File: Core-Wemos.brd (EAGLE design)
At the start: 86.5 x 100 mm, 50 parts, among them J2 CONNECTOR-GROVE-4P-2.0-347013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, J3 IO4

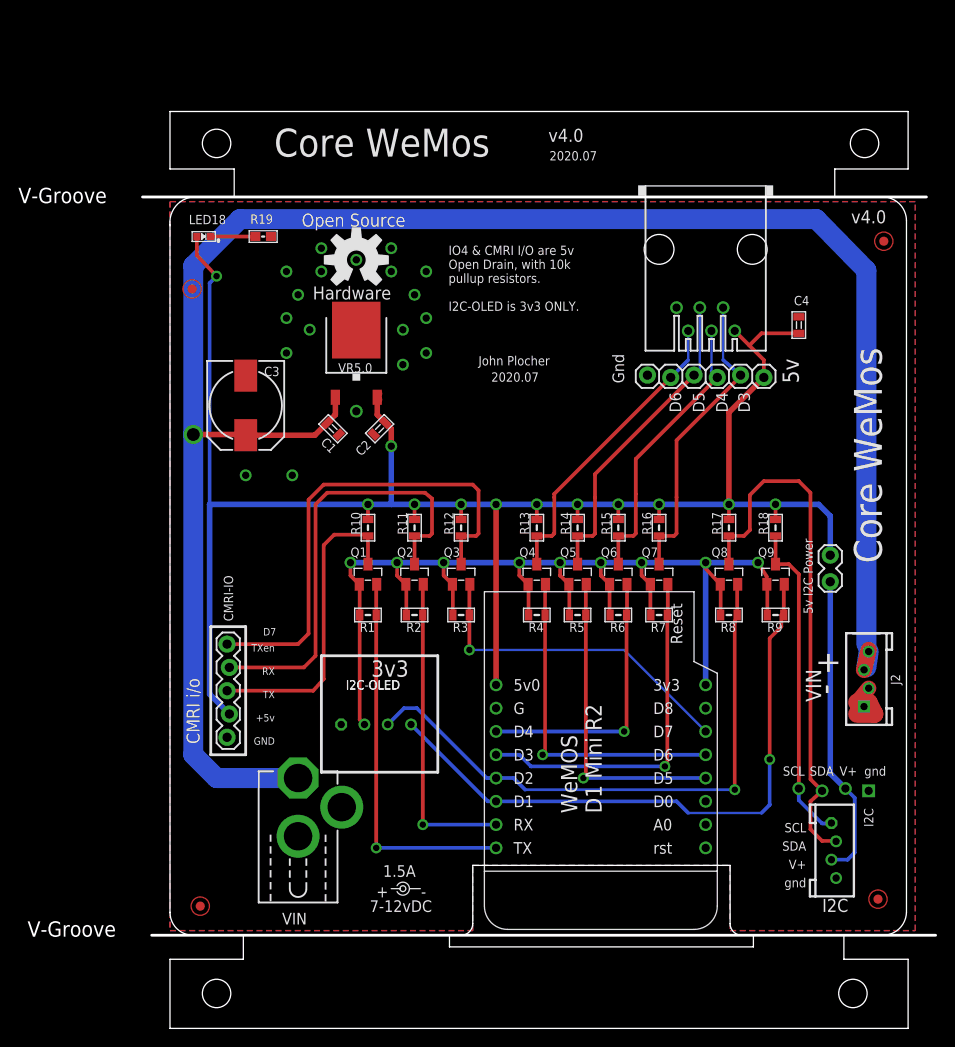
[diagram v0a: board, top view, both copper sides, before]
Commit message: Moved OLED, added 1x4 0.100 VIN
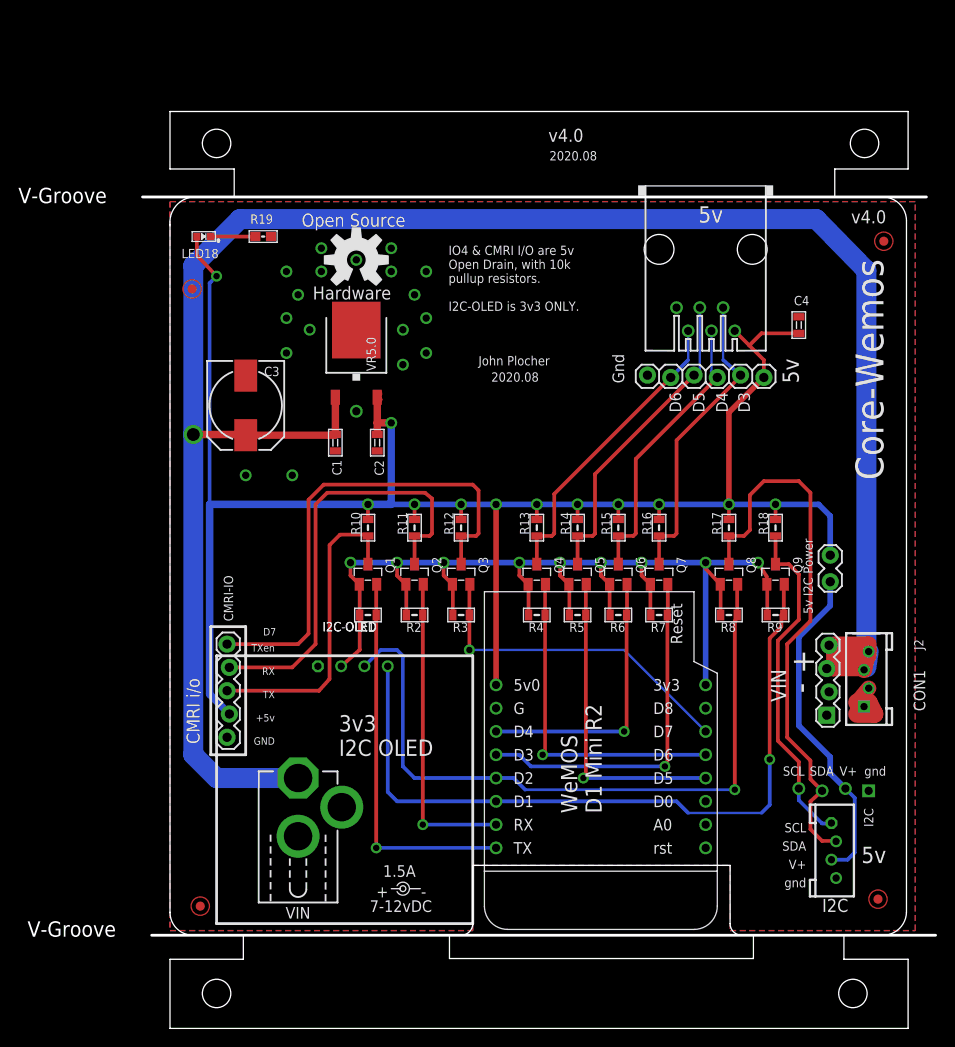
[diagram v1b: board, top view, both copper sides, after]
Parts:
- added CON1: (no value), SPCoast:1X04_LOCK
- moved I2C-OLED 6.84 mm to (19.9, 29.3)
- moved C1 1.55 mm to (18.0, 53.7), turned to 270 degrees
- moved C2 1.55 mm to (22.6, 53.7), turned to 270 degrees
- turned LED18 to 180 degrees
- turned Q1 to 270 degrees
- turned Q2 to 270 degrees
- turned Q3 to 270 degrees
- turned Q4 to 270 degrees
- turned Q5 to 270 degrees
- turned Q6 to 270 degrees
- turned Q7 to 270 degrees
- turned Q8 to 270 degrees
- turned Q9 to 270 degrees
- turned VR5.0 to 90 degrees
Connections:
- net +9V: now also CON1.3, CON1.4
- net GND: now also CON1.1, CON1.2
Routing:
- net +9V: track 208.0 -> 226.6 mm
- net SCL: track 68.3 -> 81.5 mm
- net SDA: track 65.2 -> 77.5 mm
- net +3V3: track 125.2 -> 119.6 mm
- net N$44: track 33.5 -> 36.3 mm
- net VCCIO: track 202.0 -> 204.1 mm
- net SDAH: track 58.3 -> 60.4 mm
- net SCLH: track 35.5 -> 37.4 mm
- net RXH: track 48.8 -> 48.1 mm
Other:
- board text added: "2020.08"
- board text added: "3v3 I2C OLED"
- board text added: ">DRAWING_NAME"
- board text removed: "2020.07"
- board text removed: "3v3"
- board text removed: "Core WeMos"

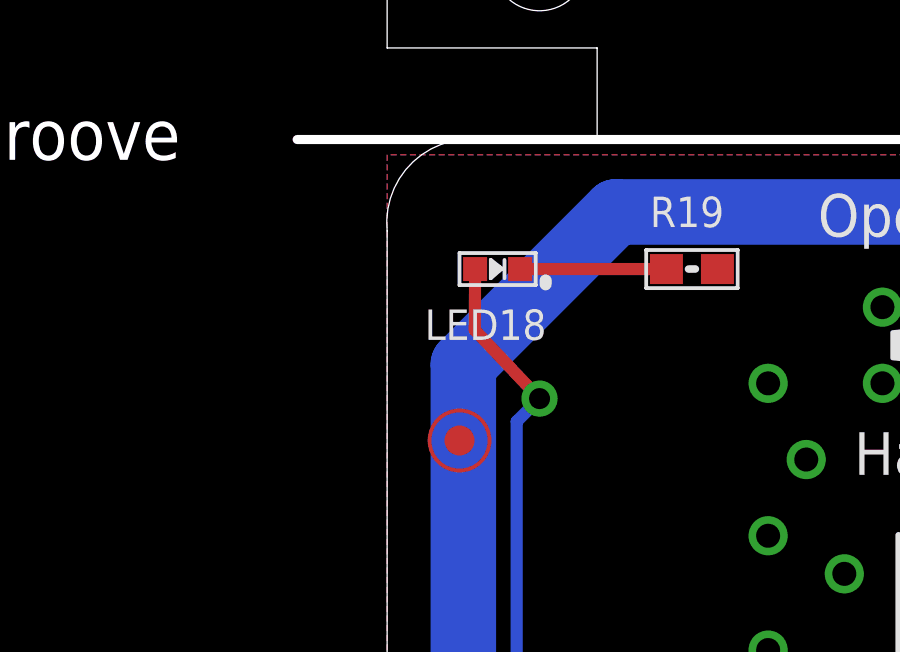
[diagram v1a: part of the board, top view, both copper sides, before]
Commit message: Renamed/Moved FIDs
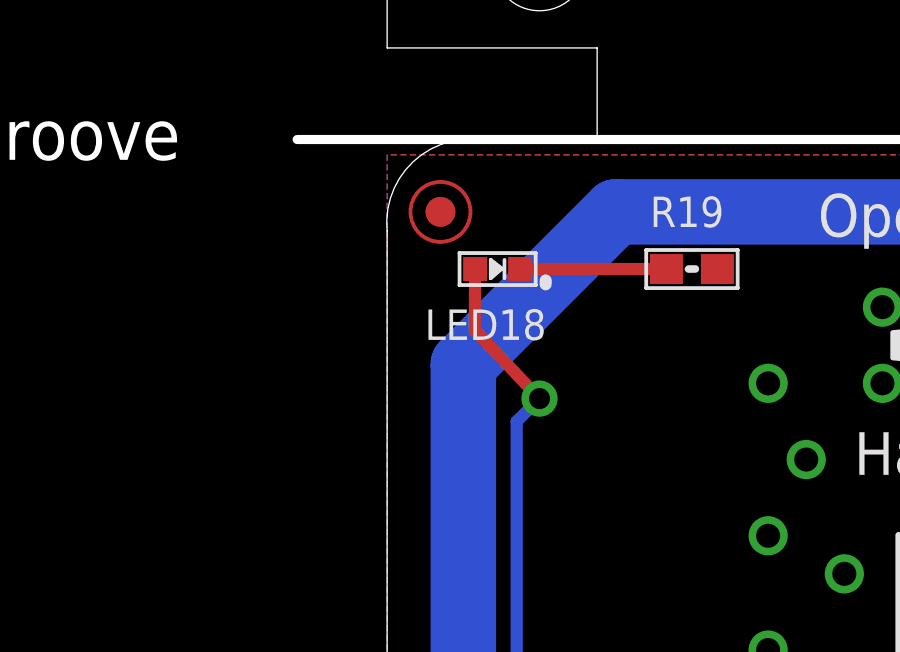
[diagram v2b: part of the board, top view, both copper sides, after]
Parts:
- removed FID3: FIDUCIAL, SPCoast:FIDUCIAL_1MM
- added FID-UL: FIDUCIAL, SPCoast:FIDUCIAL_1MM
- renumbered FID1 to FID-LR, FID2 to FID-LL, FID4 to FID-UR
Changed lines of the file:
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@@
 <setting verticaltext="up"/>
 </settings>
-<grid distance="50" unitdist="mil" unit="mil" style="dots" multiple="2" display="yes" altdistance="5" altunitdist="mil" altunit="mil"/>
+<grid distance="50" unitdist="mil" unit="mil" style="dots" multiple="2" display="yes" altdistance="25" altunitdist="mil" altunit="mil"/>
 <layers>
 <layer number="1" name="Top" color="4" fill="1" visible="yes" active="yes"/>
@@
 <attribute name="NAME" x="6.8834" y="34.2392" size="1.016" layer="25" ratio="10" rot="R90"/>
 </element>
-<element name="FID3" library="SPCoast" package="FIDUCIAL_1MM" value="FIDUCIAL" x="2.413" y="70.485" smashed="yes"/>
-<element name="FID1" library="SPCoast" package="FIDUCIAL_1MM" value="FIDUCIAL" x="77.216" y="3.937" smashed="yes"/>
-<element name="FID2" library="SPCoast" package="FIDUCIAL_1MM" value="FIDUCIAL" x="3.302" y="3.175" smashed="yes"/>
-<element name="FID4" library="SPCoast" package="FIDUCIAL_1MM" value="FIDUCIAL" x="77.851" y="75.692" smashed="yes"/>
+<element name="FID-UL" library="SPCoast" package="FIDUCIAL_1MM" value="FIDUCIAL" x="1.778" y="78.105" smashed="yes"/>
+<element name="FID-LR" library="SPCoast" package="FIDUCIAL_1MM" value="FIDUCIAL" x="77.216" y="3.937" smashed="yes"/>
+<element name="FID-LL" library="SPCoast" package="FIDUCIAL_1MM" value="FIDUCIAL" x="3.302" y="3.175" smashed="yes"/>
+<element name="FID-UR" library="SPCoast" package="FIDUCIAL_1MM" value="FIDUCIAL" x="77.851" y="75.692" smashed="yes"/>
 <element name="I2C-OLED" library="SPCoast" package="I2C-NOOUTLINE" value="" x="19.939" y="29.337" smashed="yes" rot="R180">
 <attribute name="NAME" x="16.637" y="33.147" size="1.016" layer="25" font="vector" ratio="11"/>

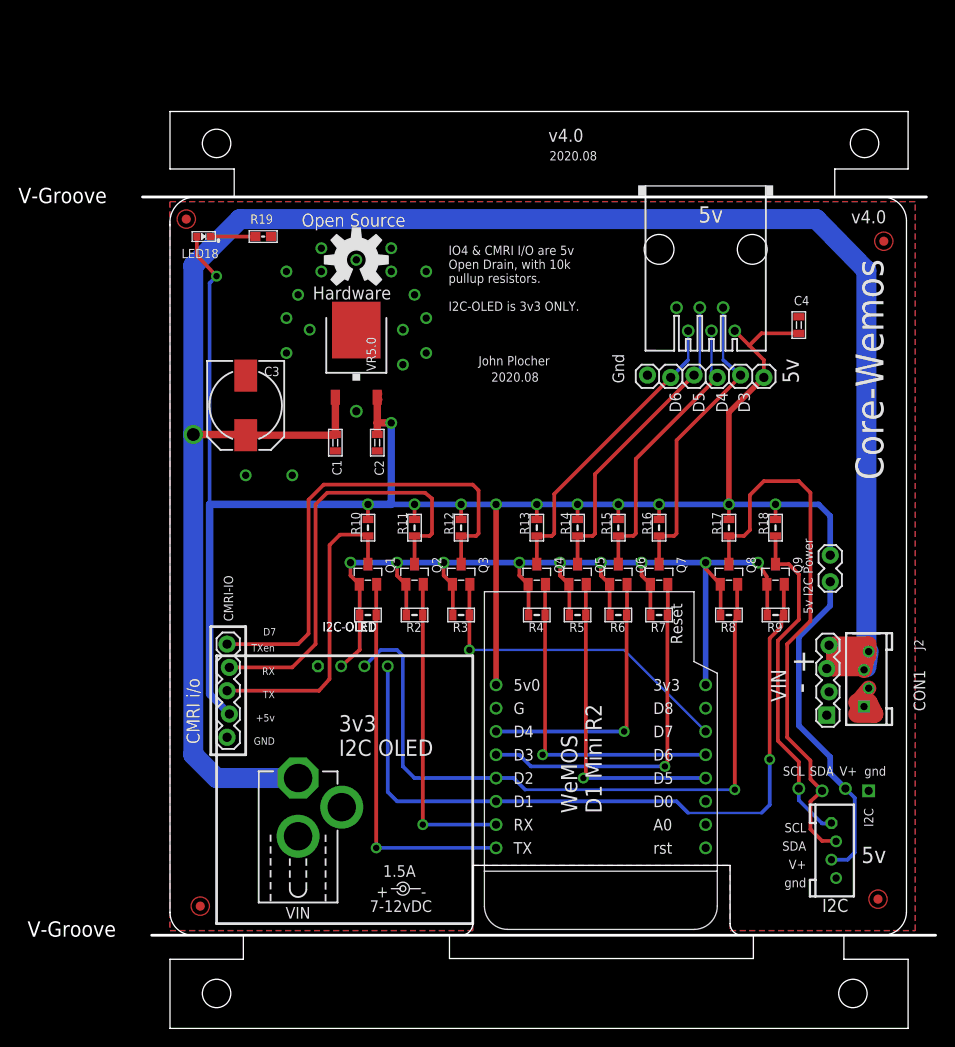
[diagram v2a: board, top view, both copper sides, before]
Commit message: Renamed/Moved FIDs
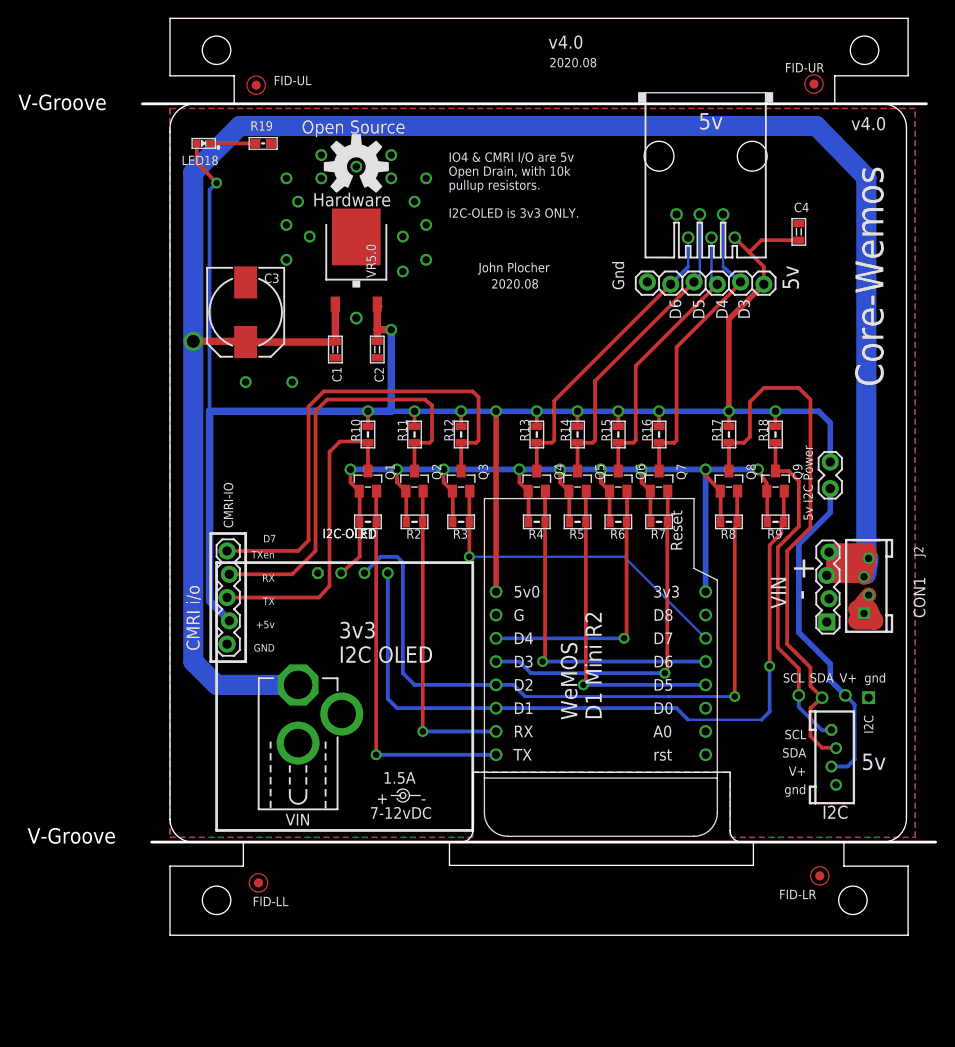
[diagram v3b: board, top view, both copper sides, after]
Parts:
- moved FID-UR 18.8 mm to (70.2, 92.8)
- moved FID-UL 16.5 mm to (9.40, 92.7)
- moved C1 10.2 mm to (18.0, 63.9)
- moved C2 10.2 mm to (22.6, 63.9)
- moved JP1 10.2 mm to (72.0, 48.9)
- moved Q1 10.2 mm to (21.6, 49.5)
- moved Q2 10.2 mm to (26.7, 49.5)
- moved Q3 10.2 mm to (31.8, 49.5)
- moved Q4 10.2 mm to (40.0, 49.5)
- moved Q5 10.2 mm to (44.5, 49.5)
- moved Q6 10.2 mm to (48.9, 49.5)
- moved Q7 10.2 mm to (53.3, 49.5)
- moved Q8 10.2 mm to (61.0, 49.5)
- moved Q9 10.2 mm to (66.0, 49.5)
- moved R1 10.2 mm to (21.6, 45.1)
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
